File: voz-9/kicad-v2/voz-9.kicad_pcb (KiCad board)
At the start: 2 copper layers, 200 x 100 mm, 199 parts, among them J1 fio 20, J2 fio 12, J3 fio 20, J4 fio 20, J5 fio 16, J6 fio 6, J7 fio 12, J8 fio 6, J9 fio 12, Q1 MMBFJ201, Q2 MMBFJ201, Q3 MMBFJ201, Q4 MMBFJ201, Q5 MMBFJ201, Q6 MMBFJ201, Q7 MMBF5457, U1 NE5532DR, U2 TL072CDR, U3 TL072CDR, U4 ICL7660, U5 78M05, U6 PT2399, U7 PT2399, U8 PT2399, U9 TL072CDR

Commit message: Fecha o roteamento da v2 200×100 mm.
As redes que o Freerouting deixou abertas entram na placa, a seda v.2 sai de cima de FONTE e o via duplicado de H2_ON sai. DRC de erros fica em zero. O zip de fabricação e o CPL acompanham a placa pronta.

Co-authored-by: Andrey <andreysenes@users.noreply.github.com>
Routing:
- net FILT_SW: track 4.11 -> 119.8 mm, vias 1 -> 2
- net SW_B: track 0.00 -> 77.7 mm, vias 0 -> 7
- net PT6_U8: track 61.4 -> 92.4 mm, vias 2 -> 4
- net U7_CC0: track 1.40 -> 20.7 mm, vias 1 -> 3
- net PT_REF_U6: track 3.77 -> 20.2 mm, vias 1 -> 2
- net ENV: track 86.0 -> 98.1 mm, vias 2 -> 3
- net GND: track 1073.0 -> 1077.6 mm, vias 8 -> 10
- net P4_TIP: track 118.8 -> 121.7 mm
- net SUM: track 135.6 -> 137.6 mm, vias 3 -> 4
- net TIME_W: track 105.9 -> 107.3 mm
- net H2_ON: vias 3 -> 2

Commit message: Deixa a v2 pronta para a JLCPCB.
Afasta a seda do cobre, tira o cobre morto sem abrir net e regenera o zip. A biblioteca dos furos de fio entra no projeto para o KiCad achar o footprint.

Co-authored-by: Andrey <andreysenes@users.noreply.github.com>
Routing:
- net TIME_W: track 107.3 -> 82.1 mm, vias 6 -> 5
- net MIDF_W: track 138.6 -> 134.8 mm, vias 4 -> 3
- net PRE_W: track 244.1 -> 240.6 mm
- net Q4G: track 25.6 -> 26.6 mm
- net U7_CC0: vias 3 -> 2
- net PITCH_CV: vias 4 -> 3
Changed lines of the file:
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@@
 		(tags "capacitor")
 		(property "Reference" "C18"
-			(at 0.94964 -1.727032 0)
+			(at 1.697056 1.697056 0)
 			(layer "F.SilkS")
 			(effects
@@
 		(tags "resistor")
 		(property "Reference" "R33"
-			(at 0 -1.65 0)
+			(at 1.015328 -2.008353 0)
 			(layer "F.SilkS")
 			(effects
@@
 		(tags "capacitor")
 		(property "Reference" "C10"
-			(at 0.307542 -2.006165 0)
+			(at -6 0 0)
 			(layer "F.SilkS")
 			(effects
@@
 		(tags "SOD-323")
 		(property "Reference" "D2"
-			(at 0 -1.85 0)
+			(at 0.043386 -2.045238 0)
 			(layer "F.SilkS")
 			(effects
@@
 		(fp_line
 			(start -1.61 -0.85)
-			(end 1.05 -0.85)
+			(end -0.771315 -0.85)
 			(stroke
 				(width 0.16)
@@
 		)
 		(fp_line
+			(start 0.371314 -0.85)
+			(end 1.05 -0.85)
+			(stroke
+				(width 0.16)
+				(type default)
+			)
+			(layer "F.SilkS")
+		)
+		(fp_line
 			(start -1.6 -0.95)
 			(end -1.6 0.95)
@@
 		(tags "resistor")
 		(property "Reference" "R24"
-			(at 0 -1.65 0)
+			(at -3.670519 -0.983513 0)
 			(layer "F.SilkS")
 			(effects
@@
 		(tags "capacitor")
 		(property "Reference" "C14"
-			(at 1.455318 -1.54593 0)
+			(at 2.68883 -1.555345 0)
 			(layer "F.SilkS")
 			(effects
@@
 	)
 	(segment
-		(start 96.5967 88.3967)
-		(end 96.5967 66.0494)
-		(width 0.2)
-		(layer "F.Cu")
-		(net "TIME_W")
-	)
-	(segment
 		(start 54.9084 58.7791)
 		(end 55 58.75)
@@
 	)
 	(segment
-		(start 98.2 90)
-		(end 96.5967 88.3967)
-		(width 0.2)
-		(layer "F.Cu")
-		(net "TIME_W")
-	)
-	(segment
 		(start 85.5 80)
 		(end 85.5 80.25)
@@
 	)
 	(segment
-		(start 96.5967 66.0494)
-		(end 97.0133 65.6328)
-		(width 0.2)
-		(layer "F.Cu")
-		(net "TIME_W")
-	)
-	(segment
 		(start 85.75 80.25)
 		(end 85.75 80.5)
@@
 	)
 	(via
-		(at 97.0133 65.6328)
-		(size 0.6)
-		(drill 0.3)
-		(layers "F.Cu" "B.Cu")
-		(net "TIME_W")
-	)
-	(via
 		(at 55 60.25)
 		(size 0.6)
@@
 	)
 	(via
-		(at 52.1918 36.3466)
-		(size 0.6)
-		(drill 0.3)
-		(layers "F.Cu" "B.Cu")
-		(net "PITCH_CV")
-	)
-	(via
 		(at 163.75 34.25)
 		(size 0.6)
@@
 	)
 	(segment
-		(start 147 24)
-		(end 132.25 24)
+		(start 132.25 24)
+		(end 133.538 23.766)
 		(width 0.2)
 		(layer "B.Cu")
@@
 	)
 	(segment
-		(start 132.25 24)
-		(end 132.25 23.75)
-		(width 0.2)
-		(layer "B.Cu")
-		(net "Q4G")
-	)
-	(segment
-		(start 132.25 23.75)
-		(end 132.304 23.7663)
+		(start 147 24)
+		(end 132.25 24)
 		(width 0.2)
 		(layer "B.Cu")
@@
 		(net "U7_CC0")
 	)
-	(via
-		(at 73.4195 47.9957)
-		(size 0.6)
-		(drill 0.3)
-		(layers "F.Cu" "B.Cu")
-		(net "U7_CC0")
-	)
 	(segment
 		(start 89.7389 48.3642)
@@
 	)
 	(segment
-		(start 88.8103 11.9603)
-		(end 88.8103 15.7728)
-		(width 0.2)
-		(layer "F.Cu")
-		(net "MIDF_W")
-	)
-	(segment
 		(start 172.75 15.5)
 		(end 172.75 15.25)
@@
 	)
 	(via
-		(at 88.8103 15.7728)
-		(size 0.6)
-		(drill 0.3)
-		(layers "F.Cu" "B.Cu")
-		(net "MIDF_W")
-	)
-	(via
 		(at 188.25 21)
 		(size 0.6)
@@
 	)
 	(segment
-		(start 52.198 44.3947)
-		(end 52.198 45.2769)
-		(width 0.2)
-		(layer "F.Cu")
-		(net "PRE_W")
-	)
-	(segment
 		(start 133.55 58.8762)
 		(end 133.55 62.4)
@@
 	)
 	(segment
-		(start 52.198 45.2769)
-		(end 52.198 44.3947)
-		(width 0.2)
-		(layer "F.Cu")
-		(net "PRE_W")
-	)
-	(segment
 		(start 48.2221 40.9197)
 		(end 51.6738 40.9197)
@@
 	)
 	(segment
-		(start 52.198 45.2769)
-		(end 52.198 44.3947)
-		(width 0.2)
-		(layer "B.Cu")
-		(net "PRE_W")
-	)
-	(segment
-		(start 52.198 44.3947)
-		(end 52.198 45.2769)
-		(width 0.2)
-		(layer "B.Cu")
-		(net "PRE_W")
-	)
-	(segment
 		(start 109.15 49.3056)
 		(end 117.62 57.7756)
@@
 		(width 0.2)
 		(layer "F.Cu")
-		(net "P4_TIP")
-	)
-	(segment
-		(start 157.75 7.5)
-		(end 157.646 7.4582)
-		(width 0.2)
-		(layer "F.Cu")

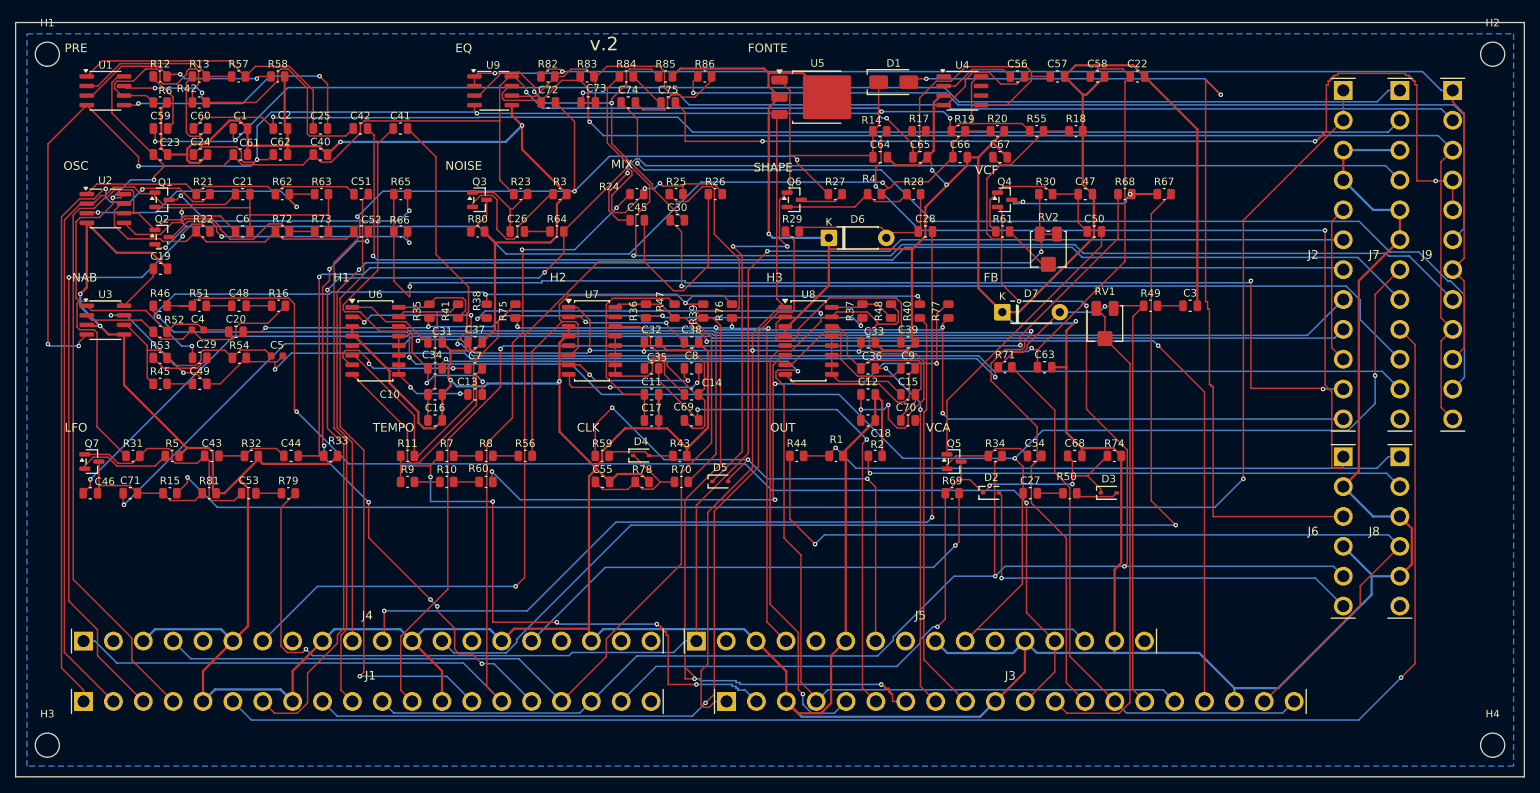
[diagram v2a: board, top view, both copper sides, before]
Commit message: Fecha os avisos de DFM da v2 para a JLCPCB.
Todas as vias ficam com anel de 0,25 mm e furo de 0,25 mm. A máscara dos furos M3 abre sem cobre, a seda sai de cima dos pads e os diodos THT se afastam do SMD. O DRC do KiCad segue zerado.

Co-authored-by: Andrey <andreysenes@users.noreply.github.com>
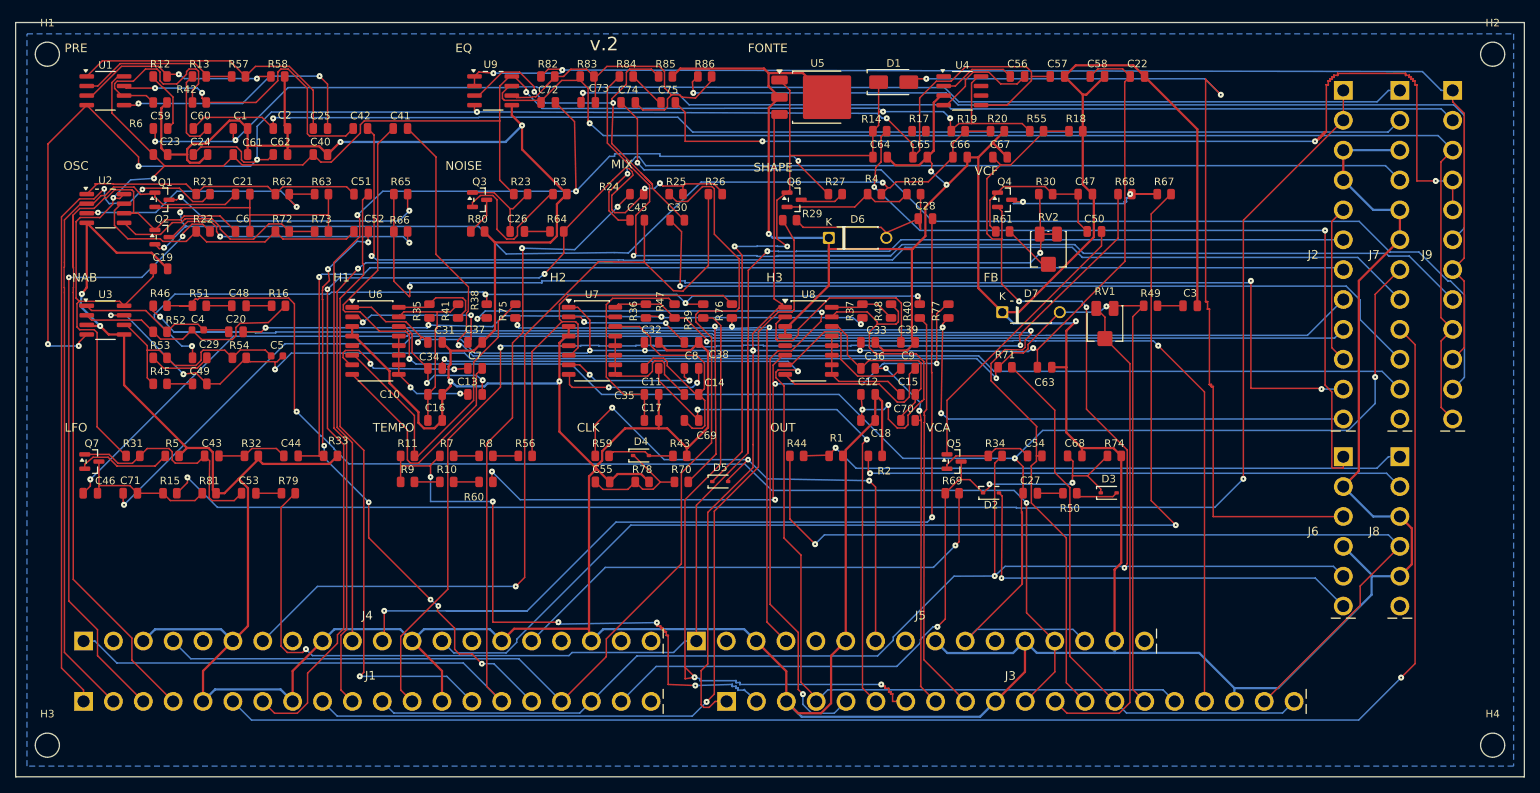
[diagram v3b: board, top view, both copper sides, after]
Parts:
- moved C28 1.70 mm to (120.6, 26.0)
- moved R29 1.54 mm to (102.6, 26.2)
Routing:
- net MIDG_W: track 139.8 -> 155.2 mm
- net LFO_OUT: track 210.4 -> 222.9 mm
- net FILT_SW: track 119.8 -> 132.3 mm
- net DRY: track 177.6 -> 188.9 mm
- net PRE_W: track 240.6 -> 250.4 mm
- net MIDF_W: track 134.8 -> 143.9 mm
- net U2B_INM: track 99.6 -> 106.8 mm
- net TIME_W: track 82.1 -> 86.4 mm
- net H2_ON: track 85.8 -> 88.3 mm
- net EQ_SUM: track 43.5 -> 46.0 mm
- net EQ_IN: track 50.8 -> 53.2 mm
- net SHAPE: track 22.1 -> 24.4 mm
- net P4_TIP: track 121.6 -> 123.4 mm
- net PITCH_CV: track 155.1 -> 156.7 mm
- net SHAPE_W: track 121.2 -> 122.7 mm
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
